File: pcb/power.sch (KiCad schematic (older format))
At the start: 0 parts

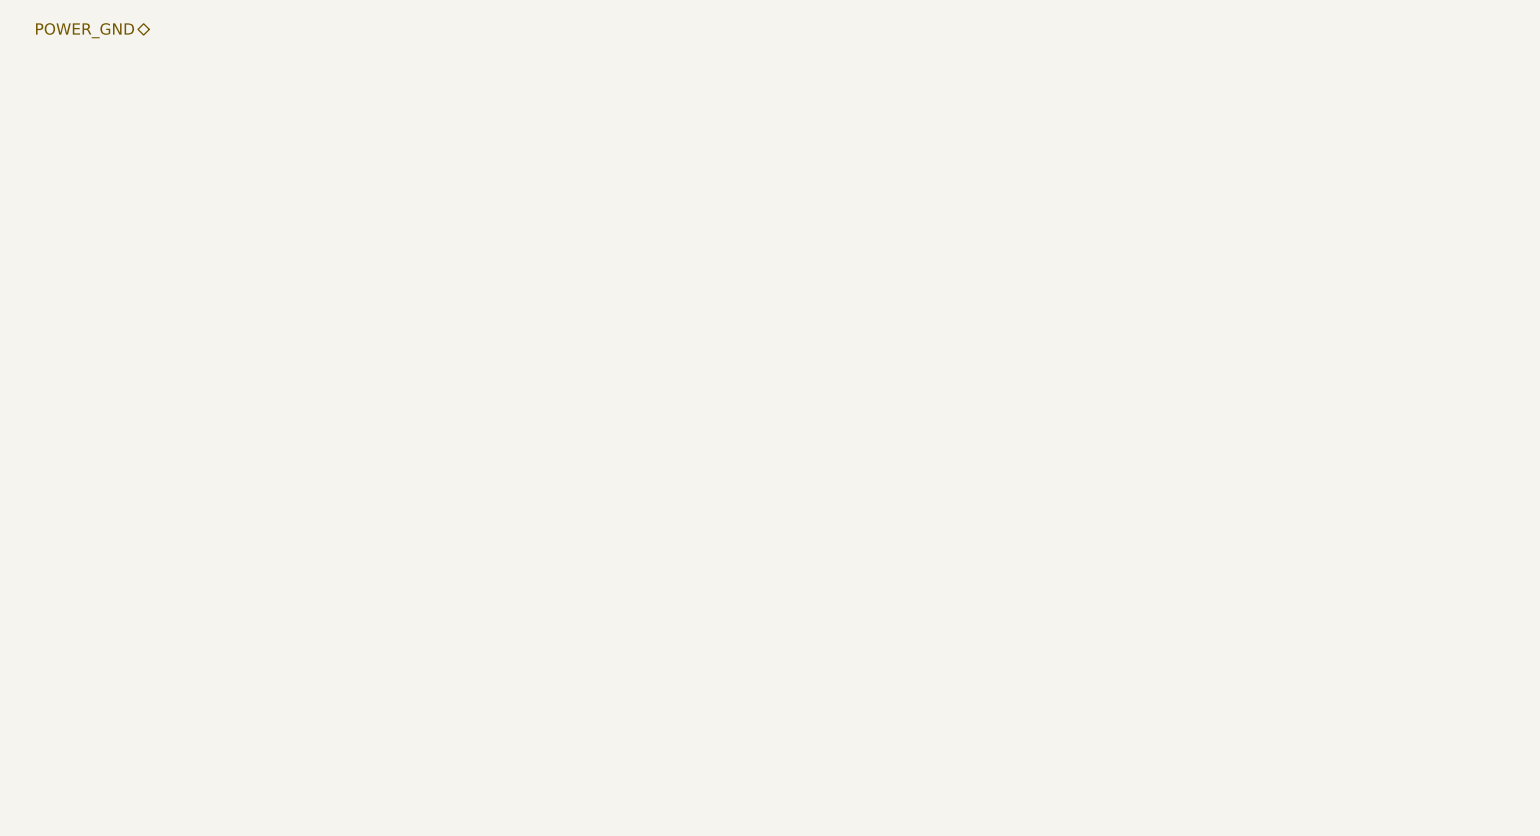
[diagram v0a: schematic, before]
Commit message: buffer section finished, audio moved to expansion connector
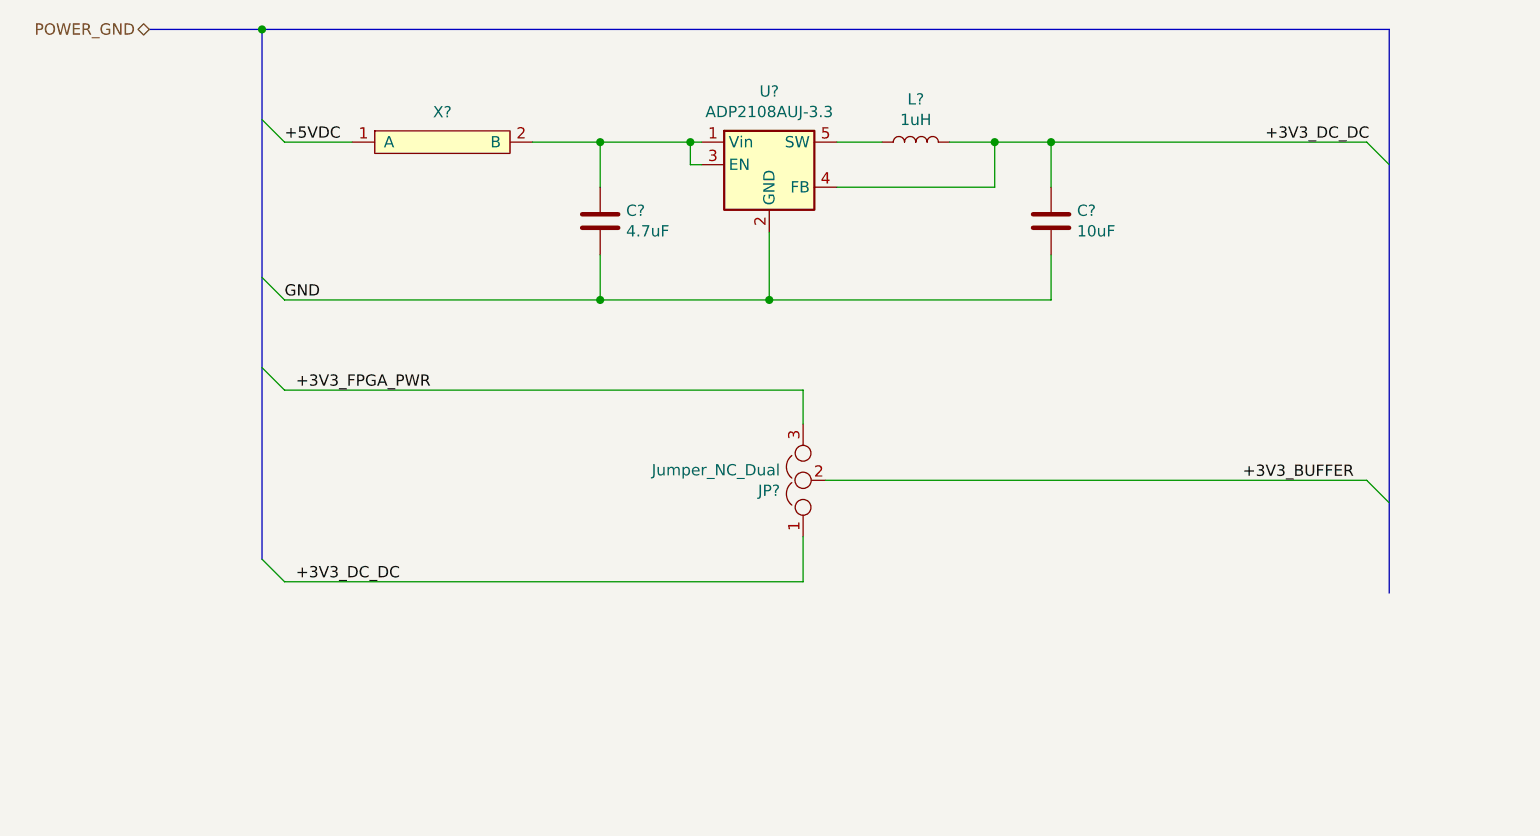
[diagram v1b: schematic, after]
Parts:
- added C?: 4.7uF, symbol Device:C
- added C?: 10uF, symbol Device:C
- added JP?: Jumper_NC_Dual, symbol Device:Jumper_NC_Dual
- added L?: 1uH, symbol Device:L
- added U?: ADP2108AUJ-3.3, Package_TO_SOT_SMD:TSOT-23-5, symbol Regulator_Switching:ADP2108AUJ-3.3
- added X?: testpoint_cutline, symbol WM1200:testpoint_cutline
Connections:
- new net: C?.1, U?.1 (Vin), U?.3 (EN), X?.2 (B)
- new net: L?.1, U?.5 (SW)
- new net +3V3_BUFFER: JP?.2
- new net +3V3_DC_DC: C?.1, JP?.1, L?.2, U?.4 (FB)
- new net +3V3_FPGA_PWR: JP?.3
- new net +5VDC: X?.1 (A)
- new net GND: C?.2, C?.2, U?.2 (GND)
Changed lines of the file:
@@
 Text HLabel 1000 1500 0    50   BiDi ~ 0
 POWER_GND
+$Comp
+L Regulator_Switching:ADP2108AUJ-3.3 U?
+U 1 1 5E713D7E
+P 3750 2100
+F 0 "U?" H 3750 2425 50  0000 C CNN
+F 1 "ADP2108AUJ-3.3" H 3750 2334 50  0000 C CNN
+F 2 "Package_TO_SOT_SMD:TSOT-23-5" H 3800 1850 50  0001 L CNN
+F 3 "https://www.analog.com/media/en/technical-documentation/data-sheets/ADP2108.pdf" H 3500 1750 50  0001 C CNN
+	1    3750 2100
+	1    0    0    -1
+$EndComp
+Wire Bus Line
+	1000 1500 1500 1500
+Entry Wire Line
+	1500 1900 1600 2000
+$Comp
+L WM1200:testpoint_cutline X?
+U 1 1 5E716612
+P 2300 2050
+F 0 "X?" H 2300 2233 50  0000 C CNN
+F 1 "testpoint_cutline" H 2300 2200 50  0001 C CNN
+F 2 "" H 2450 2050 50  0001 C CNN
+F 3 "" H 2450 2050 50  0001 C CNN
+	1    2300 2050
+	1    0    0    -1
+$EndComp
+Wire Wire Line
+	1600 2000 1900 2000
+Wire Wire Line
+	2700 2000 3000 2000
+Wire Wire Line
+	3450 2100 3400 2100
+Wire Wire Line
+	3400 2100 3400 2000
+Connection ~ 3400 2000
+Wire Wire Line
+	3400 2000 3450 2000
+Text Label 1600 2000 0    50   ~ 0
++5VDC
+$Comp
+L Device:C C?
+U 1 1 5E718DCB
+P 3000 2350
+F 0 "C?" H 3115 2396 50  0000 L CNN
+F 1 "4.7uF" H 3115 2305 50  0000 L CNN
+F 2 "" H 3038 2200 50  0001 C CNN
+F 3 "~" H 3000 2350 50  0001 C CNN
+	1    3000 2350
+	1    0    0    -1
+$EndComp
+Entry Wire Line
+	1500 2600 1600 2700
+Wire Wire Line
+	1600 2700 3000 2700
+Wire Wire Line
+	3000 2700 3000 2500
+Wire Wire Line
+	3000 2200 3000 2000
+Connection ~ 3000 2000
+Wire Wire Line
+	3000 2000 3400 2000
+Text Label 1600 2700 0    50   ~ 0
+GND
+Wire Bus Line
+	1500 1500 6500 1500
+Connection ~ 1500 1500
+$Comp
+L Device:C C?
+U 1 1 5E71F97C
+P 5000 2350
+F 0 "C?" H 5115 2396 50  0000 L CNN
+F 1 "10uF" H 5115 2305 50  0000 L CNN
+F 2 "" H 5038 2200 50  0001 C CNN
+F 3 "~" H 5000 2350 50  0001 C CNN
+	1    5000 2350
+	1    0    0    -1
+$EndComp
+Wire Wire Line
+	5000 2700 5000 2500
+Wire Wire Line
+	3000 2700 3750 2700
+Connection ~ 3000 2700
+Entry Wire Line
+	6400 2000 6500 2100
+Wire Wire Line
+	5000 2200 5000 2000
+Wire Wire Line
+	5000 2000 6400 2000
+$Comp
+L Device:L L?
+U 1 1 5E72022D
+P 4400 2000
+F 0 "L?" V 4590 2000 50  0000 C CNN
+F 1 "1uH" V 4499 2000 50  0000 C CNN
+F 2 "" H 4400 2000 50  0001 C CNN
+F 3 "~" H 4400 2000 50  0001 C CNN
+	1    4400 2000
+	0    -1   -1   0
+$EndComp
+Wire Wire Line
+	4050 2200 4750 2200
+Wire Wire Line
+	4750 2200 4750 2000
+Wire Wire Line
+	4750 2000 5000 2000
+Connection ~ 5000 2000
+Wire Wire Line
+	4550 2000 4750 2000
+Connection ~ 4750 2000
+Wire Wire Line
+	4050 2000 4250 2000
+Wire Wire Line
+	3750 2400 3750 2700
+Connection ~ 3750 2700
+Wire Wire Line
+	3750 2700 5000 2700
+Text Label 5950 2000 0    50   ~ 0
++3V3_DC_DC
+$Comp
+L Device:Jumper_NC_Dual JP?
+U 1 1 5E722973
+P 3900 3500
+F 0 "JP?" V 3854 3602 50  0000 L CNN
+F 1 "Jumper_NC_Dual" V 3945 3602 50  0000 L CNN
+F 2 "" H 3900 3500 50  0001 C CNN
+F 3 "~" H 3900 3500 50  0001 C CNN
+	1    3900 3500
+	0    -1   -1   0
+$EndComp
+Entry Wire Line
+	1500 3000 1600 3100
+Entry Wire Line
+	1500 3850 1600 3950
+Entry Wire Line
+	6400 3500 6500 3600
+Wire Wire Line
+	3900 3250 3900 3100
+Wire Wire Line
+	3900 3100 1600 3100
+Wire Wire Line
+	3900 3750 3900 3950
+Wire Wire Line
+	3900 3950 1600 3950
+Text Label 1650 3950 0    50   ~ 0
++3V3_DC_DC
+Text Label 1650 3100 0    50   ~ 0
++3V3_FPGA_PWR
+Wire Wire Line
+	4000 3500 6400 3500
+Wire Bus Line
+	6500 1500 6500 4000
+Wire Bus Line
+	1500 1500 1500 3850
+Text Label 5850 3500 0    50   ~ 0
++3V3_BUFFER
 $EndSCHEMATC

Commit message: Some work done on the whole project
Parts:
- added JP2: Jumper, symbol Device:Jumper
- gave numbers to parts that had none: 6
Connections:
- net +5VDC: now also JP2.1
- net +3V3_FPGA_PWR renamed FPGA_VCC3V3
- new net FPGA_VCC5V: JP2.2
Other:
- note added: "Jumper selects FPGA Devboard power source\nOpen: FPGA Devboard gets 5V from usb or from DC connector\nClose: FPGA Devboard gets 5V from Amiga"
- note added: "Jumper selects buffer power source:\n1-2: DC-DC converter onboard\n2-3: 3V3 from FPGA Devboard\nOpen: no power on buffers"
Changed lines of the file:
@@
 $Descr A4 11693 8268
 encoding utf-8
-Sheet 11 11
+Sheet 10 11
 Title "WishMaster 1200"
 Date ""
@@
 POWER_GND
 $Comp
-L Regulator_Switching:ADP2108AUJ-3.3 U?
+L Regulator_Switching:ADP2108AUJ-3.3 U6
 U 1 1 5E713D7E
 P 3750 2100
-F 0 "U?" H 3750 2425 50  0000 C CNN
+F 0 "U6" H 3750 2425 50  0000 C CNN
 F 1 "ADP2108AUJ-3.3" H 3750 2334 50  0000 C CNN
 F 2 "Package_TO_SOT_SMD:TSOT-23-5" H 3800 1850 50  0001 L CNN
@@
 	1500 1900 1600 2000
 $Comp
-L WM1200:testpoint_cutline X?
+L WM1200:testpoint_cutline X4
 U 1 1 5E716612
 P 2300 2050
-F 0 "X?" H 2300 2233 50  0000 C CNN
+F 0 "X4" H 2300 2233 50  0000 C CNN
 F 1 "testpoint_cutline" H 2300 2200 50  0001 C CNN
 F 2 "" H 2450 2050 50  0001 C CNN
@@
 +5VDC
 $Comp
-L Device:C C?
+L Device:C C11
 U 1 1 5E718DCB
 P 3000 2350
-F 0 "C?" H 3115 2396 50  0000 L CNN
+F 0 "C11" H 3115 2396 50  0000 L CNN
 F 1 "4.7uF" H 3115 2305 50  0000 L CNN
 F 2 "" H 3038 2200 50  0001 C CNN
@@
 Connection ~ 1500 1500
 $Comp
-L Device:C C?
+L Device:C C12
 U 1 1 5E71F97C
 P 5000 2350
-F 0 "C?" H 5115 2396 50  0000 L CNN
+F 0 "C12" H 5115 2396 50  0000 L CNN
 F 1 "10uF" H 5115 2305 50  0000 L CNN
 F 2 "" H 5038 2200 50  0001 C CNN
@@
 	5000 2000 6400 2000
 $Comp
-L Device:L L?
+L Device:L L1
 U 1 1 5E72022D
 P 4400 2000
-F 0 "L?" V 4590 2000 50  0000 C CNN
+F 0 "L1" V 4590 2000 50  0000 C CNN
 F 1 "1uH" V 4499 2000 50  0000 C CNN
 F 2 "" H 4400 2000 50  0001 C CNN
@@
 +3V3_DC_DC
 $Comp
-L Device:Jumper_NC_Dual JP?
+L Device:Jumper_NC_Dual JP1
 U 1 1 5E722973
 P 3900 3500
-F 0 "JP?" V 3854 3602 50  0000 L CNN
+F 0 "JP1" V 3854 3602 50  0000 L CNN
 F 1 "Jumper_NC_Dual" V 3945 3602 50  0000 L CNN
 F 2 "" H 3900 3500 50  0001 C CNN
@@
 +3V3_DC_DC
 Text Label 1650 3100 0    50   ~ 0
-+3V3_FPGA_PWR
+FPGA_VCC3V3
 Wire Wire Line
 	4000 3500 6400 3500
-Wire Bus Line
-	6500 1500 6500 4000
-Wire Bus Line
-	1500 1500 1500 3850
 Text Label 5850 3500 0    50   ~ 0
 +3V3_BUFFER
+$Comp
+L Device:Jumper JP2
+U 1 1 5E7037DF
+P 3900 4500
+F 0 "JP2" H 3900 4764 50  0000 C CNN
+F 1 "Jumper" H 3900 4673 50  0000 C CNN
+F 2 "" H 3900 4500 50  0001 C CNN
+F 3 "~" H 3900 4500 50  0001 C CNN
+	1    3900 4500
+	1    0    0    -1
+$EndComp
+Entry Wire Line
+	1500 4400 1600 4500
+Entry Wire Line
+	6400 4500 6500 4600
+Wire Wire Line
+	1600 4500 3600 4500
+Wire Wire Line
+	4200 4500 6400 4500
+Text Label 1650 4500 0    50   ~ 0
++5VDC
+Text Label 5900 4500 0    50   ~ 0
+FPGA_VCC5V
+Text Notes 4000 3850 0    50   ~ 0
+Jumper selects buffer power source:\n1-2: DC-DC converter onboard\n2-3: 3V3 from FPGA Devboard\nOpen: no power on buffers
+Text Notes 3000 4850 0    50   ~ 0
+Jumper selects FPGA Devboard power source\nOpen: FPGA Devboard gets 5V from usb or from DC connector\nClose: FPGA Devboard gets 5V from Amiga
+Wire Bus Line
+	6500 1500 6500 5000
+Wire Bus Line
+	1500 1500 1500 5000
 $EndSCHEMATC

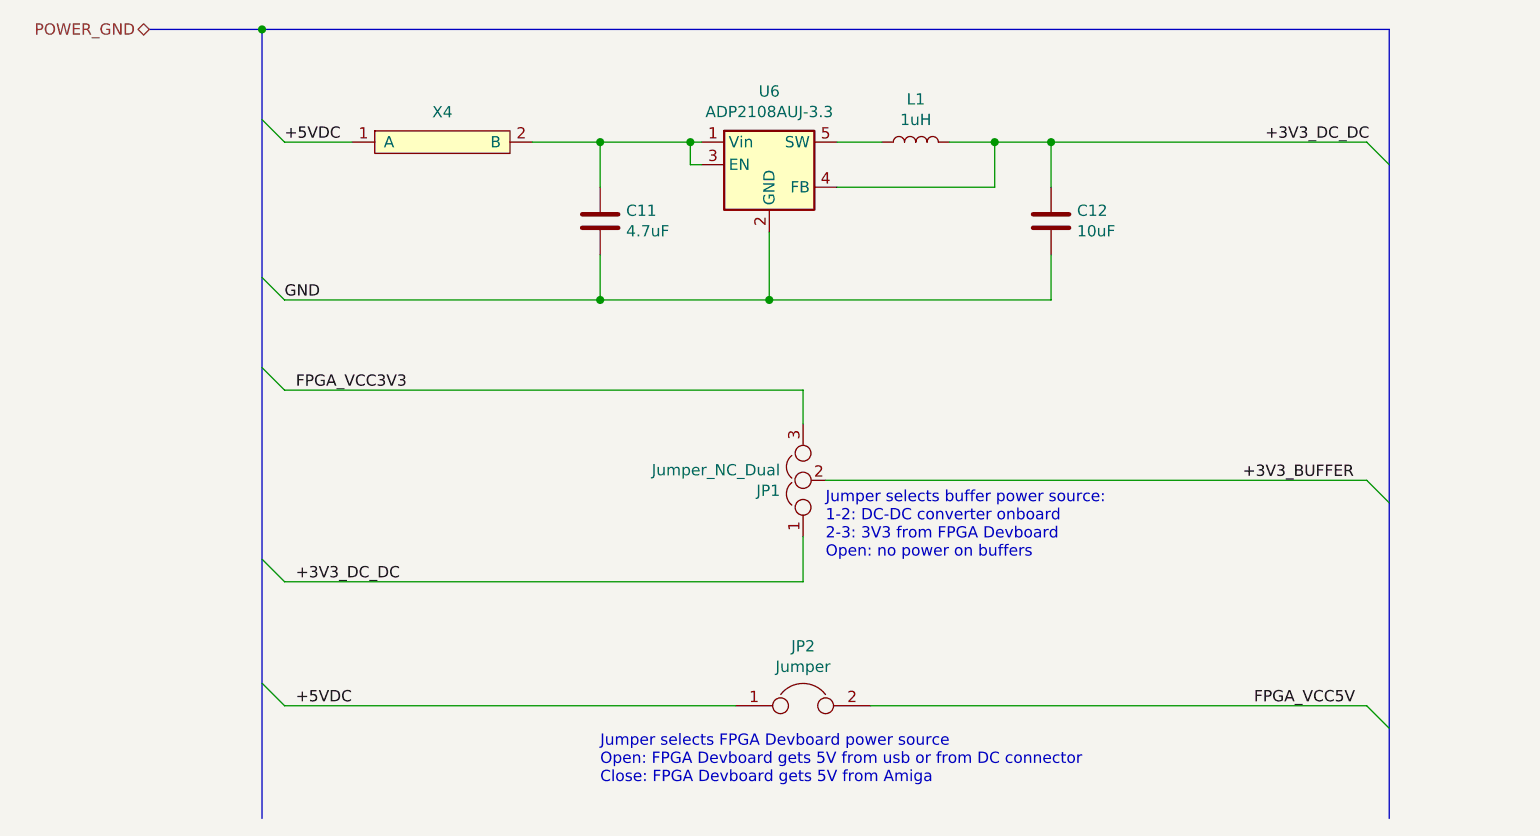
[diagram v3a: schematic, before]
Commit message: ok, we are using global labels now
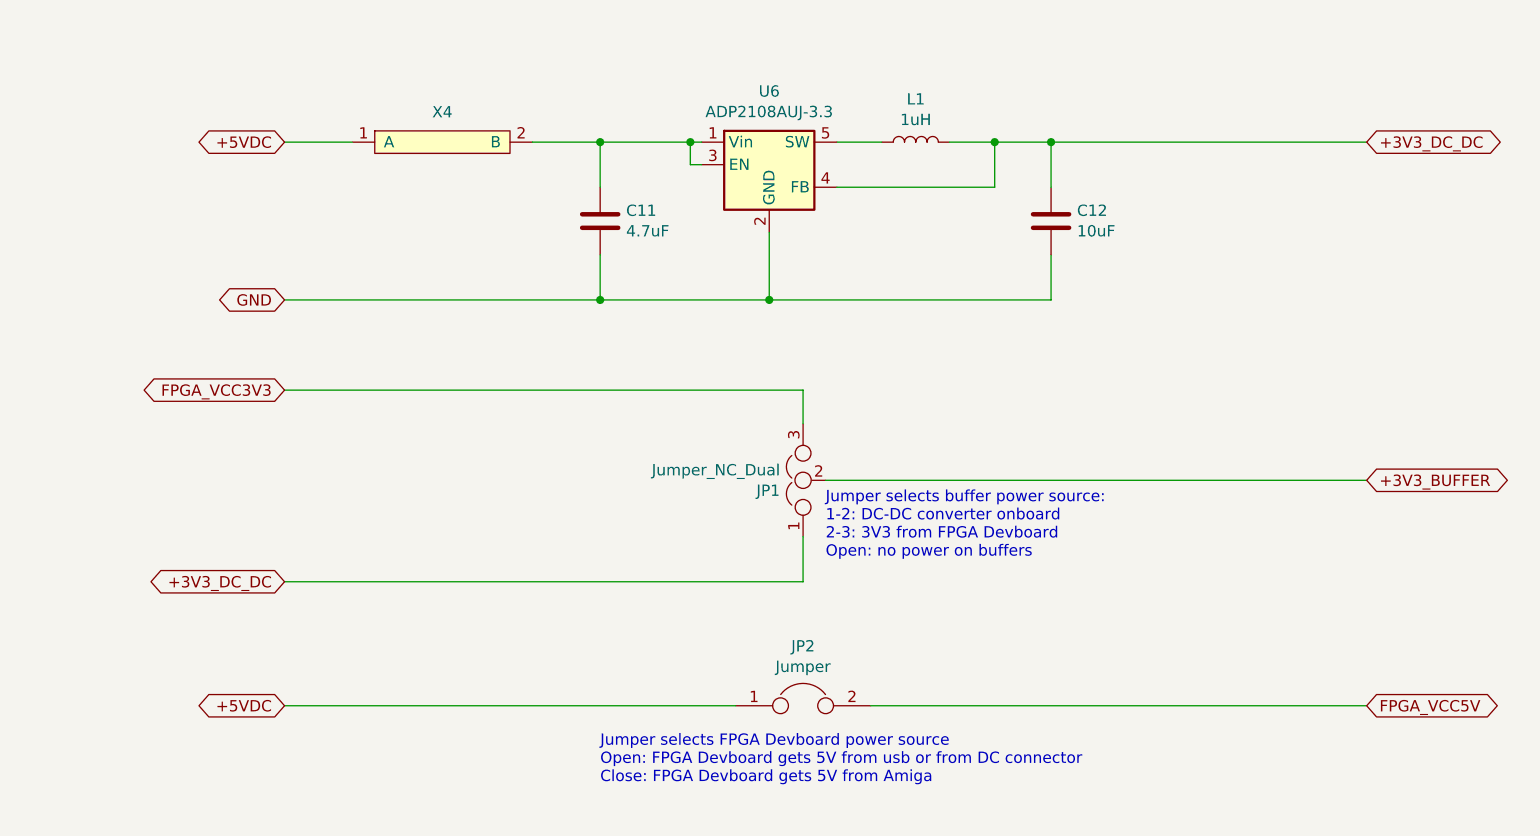
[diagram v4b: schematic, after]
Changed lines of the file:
@@
 $Descr A4 11693 8268
 encoding utf-8
-Sheet 10 11
+Sheet 6 11
 Title "WishMaster 1200"
 Date ""
@@
 Comment4 ""
 $EndDescr
-Text HLabel 1000 1500 0    50   BiDi ~ 0
-POWER_GND
 $Comp
 L Regulator_Switching:ADP2108AUJ-3.3 U6
@@
 	1    0    0    -1
 $EndComp
-Wire Bus Line
-	1000 1500 1500 1500
-Entry Wire Line
-	1500 1900 1600 2000
 $Comp
 L WM1200:testpoint_cutline X4
@@
 Wire Wire Line
 	3400 2000 3450 2000
-Text Label 1600 2000 0    50   ~ 0
-+5VDC
 $Comp
 L Device:C C11
@@
 	1    0    0    -1
 $EndComp
-Entry Wire Line
-	1500 2600 1600 2700
 Wire Wire Line
 	1600 2700 3000 2700
@@
 Wire Wire Line
 	3000 2000 3400 2000
-Text Label 1600 2700 0    50   ~ 0
-GND
-Wire Bus Line
-	1500 1500 6500 1500
-Connection ~ 1500 1500
 $Comp
 L Device:C C12
@@
 	3000 2700 3750 2700
 Connection ~ 3000 2700
-Entry Wire Line
-	6400 2000 6500 2100
 Wire Wire Line
 	5000 2200 5000 2000
@@
 Wire Wire Line
 	3750 2700 5000 2700
-Text Label 5950 2000 0    50   ~ 0
-+3V3_DC_DC
 $Comp
 L Device:Jumper_NC_Dual JP1
@@
 	0    -1   -1   0
 $EndComp
-Entry Wire Line
-	1500 3000 1600 3100
-Entry Wire Line
-	1500 3850 1600 3950
-Entry Wire Line
-	6400 3500 6500 3600
 Wire Wire Line
 	3900 3250 3900 3100
@@
 Wire Wire Line
 	3900 3950 1600 3950
-Text Label 1650 3950 0    50   ~ 0
-+3V3_DC_DC
-Text Label 1650 3100 0    50   ~ 0
-FPGA_VCC3V3
 Wire Wire Line
 	4000 3500 6400 3500
-Text Label 5850 3500 0    50   ~ 0
-+3V3_BUFFER
 $Comp
 L Device:Jumper JP2
@@
 	1    0    0    -1
 $EndComp
-Entry Wire Line
-	1500 4400 1600 4500
-Entry Wire Line
-	6400 4500 6500 4600
 Wire Wire Line
 	1600 4500 3600 4500
 Wire Wire Line
 	4200 4500 6400 4500
-Text Label 1650 4500 0    50   ~ 0
-+5VDC
-Text Label 5900 4500 0    50   ~ 0
-FPGA_VCC5V
 Text Notes 4000 3850 0    50   ~ 0
 Jumper selects buffer power source:\n1-2: DC-DC converter onboard\n2-3: 3V3 from FPGA Devboard\nOpen: no power on buffers
 Text Notes 3000 4850 0    50   ~ 0
 Jumper selects FPGA Devboard power source\nOpen: FPGA Devboard gets 5V from usb or from DC connector\nClose: FPGA Devboard gets 5V from Amiga
-Wire Bus Line
-	6500 1500 6500 5000
-Wire Bus Line
-	1500 1500 1500 5000
+Text GLabel 1600 2000 0    50   BiDi ~ 0
++5VDC
+Text GLabel 1600 2700 0    50   BiDi ~ 0
+GND
+Text GLabel 6400 2000 2    50   BiDi ~ 0
++3V3_DC_DC
+Text GLabel 1600 3100 0    50   BiDi ~ 0
+FPGA_VCC3V3
+Text GLabel 1600 3950 0    50   BiDi ~ 0
++3V3_DC_DC
+Text GLabel 1600 4500 0    50   BiDi ~ 0
++5VDC
+Text GLabel 6400 3500 2    50   BiDi ~ 0
++3V3_BUFFER
+Text GLabel 6400 4500 2    50   BiDi ~ 0
+FPGA_VCC5V
 $EndSCHEMATC

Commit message: fpga-side gpio connector added
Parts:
- renumbered X4 to X1
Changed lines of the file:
@@
 $EndComp
 $Comp
-L WM1200:testpoint_cutline X4
+L WM1200:testpoint_cutline X1
 U 1 1 5E716612
 P 2300 2050
-F 0 "X4" H 2300 2233 50  0000 C CNN
+F 0 "X1" H 2300 2233 50  0000 C CNN
 F 1 "testpoint_cutline" H 2300 2200 50  0001 C CNN
 F 2 "" H 2450 2050 50  0001 C CNN

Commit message: testpoints footprints added, some footprints assigned
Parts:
- renumbered X1 to XT?
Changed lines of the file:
@@
 $EndComp
 $Comp
-L WM1200:testpoint_cutline X1
+L WM1200:testpoint_cutline XT?
 U 1 1 5E716612
 P 2300 2050
-F 0 "X1" H 2300 2233 50  0000 C CNN
+F 0 "XT?" H 2300 2233 50  0000 C CNN
 F 1 "testpoint_cutline" H 2300 2200 50  0001 C CNN
 F 2 "" H 2450 2050 50  0001 C CNN

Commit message: more footprints assigned
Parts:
- JP1: footprint (none) -> Connector_PinSocket_2.54mm:PinSocket_1x03_P2.54mm_Vertical
- JP2: footprint (none) -> Connector_PinSocket_2.54mm:PinSocket_1x02_P2.54mm_Vertical
- XT55: renamed from XT?; footprint (none) -> WM1200:testpoint_cutline
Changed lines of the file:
@@
 $EndComp
 $Comp
-L WM1200:testpoint_cutline XT?
+L WM1200:testpoint_cutline XT55
 U 1 1 5E716612
 P 2300 2050
-F 0 "XT?" H 2300 2233 50  0000 C CNN
+F 0 "XT55" H 2300 2233 50  0000 C CNN
 F 1 "testpoint_cutline" H 2300 2200 50  0001 C CNN
-F 2 "" H 2450 2050 50  0001 C CNN
+F 2 "WM1200:testpoint_cutline" H 2450 2050 50  0001 C CNN
 F 3 "" H 2450 2050 50  0001 C CNN
 	1    2300 2050
@@
 F 0 "JP1" V 3854 3602 50  0000 L CNN
 F 1 "Jumper_NC_Dual" V 3945 3602 50  0000 L CNN
-F 2 "" H 3900 3500 50  0001 C CNN
+F 2 "Connector_PinSocket_2.54mm:PinSocket_1x03_P2.54mm_Vertical" H 3900 3500 50  0001 C CNN
 F 3 "~" H 3900 3500 50  0001 C CNN
 	1    3900 3500
@@
 F 0 "JP2" H 3900 4764 50  0000 C CNN
 F 1 "Jumper" H 3900 4673 50  0000 C CNN
-F 2 "" H 3900 4500 50  0001 C CNN
+F 2 "Connector_PinSocket_2.54mm:PinSocket_1x02_P2.54mm_Vertical" H 3900 4500 50  0001 C CNN
 F 3 "~" H 3900 4500 50  0001 C CNN
 	1    3900 4500
